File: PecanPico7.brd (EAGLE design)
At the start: 34.2 x 50 mm, 130 parts, among them IC1 Si4464-B1B-FM, IC10 TC1185-1.8VCT713, IC11 TC1185-2.5VCT713, IC12 ADR380ARTZ, IC13 AVT-55689, IC2 Si4464-B1B-FM, IC3 BME280_BME280, IC4 UBLOX_MAX-6, IC5 STM32F429IIH6, IC6 TPS61202, IC7 SPV1040, IC8 TXC_7Z, IC9 TPS62260DRVT, Q1 AP2301, U2 PAC1720-1-AIA-TR, X1 CAMERA_HEADER

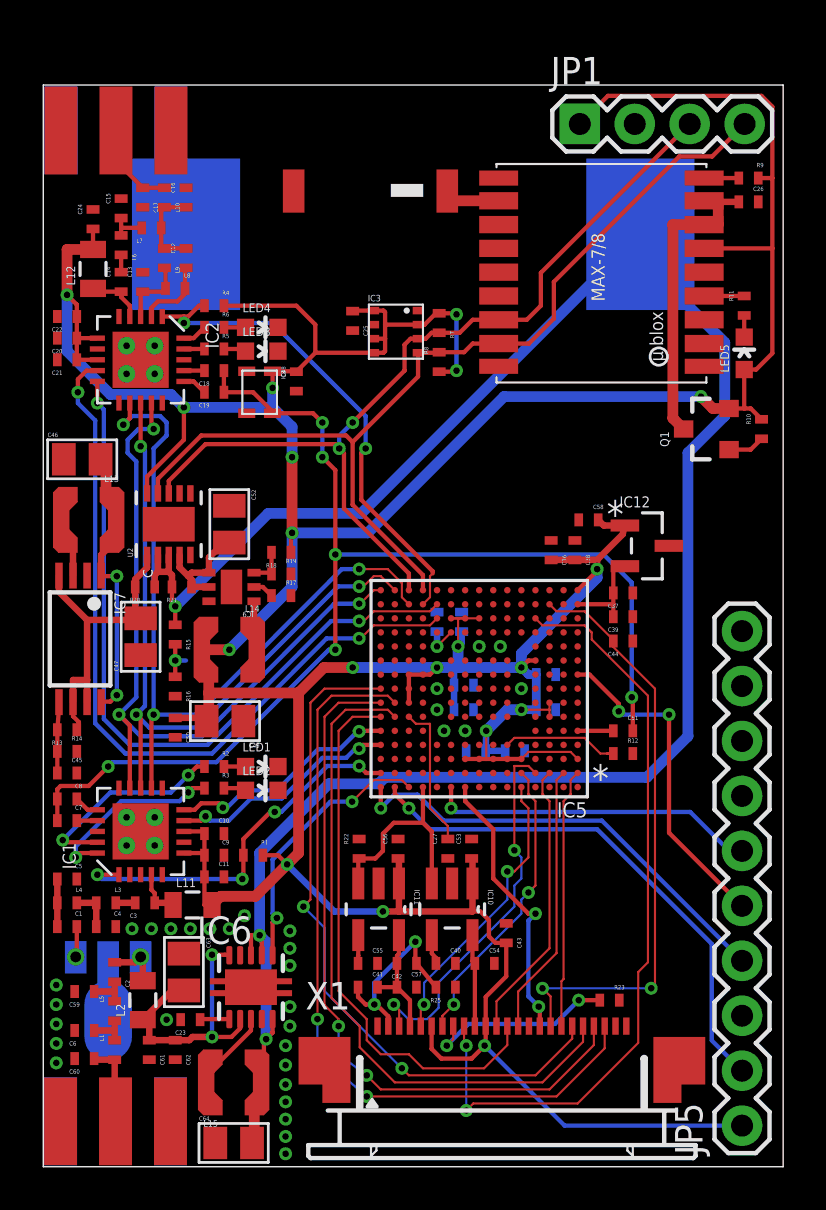
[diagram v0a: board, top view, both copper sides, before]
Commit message: Added RF6886, moved parts around
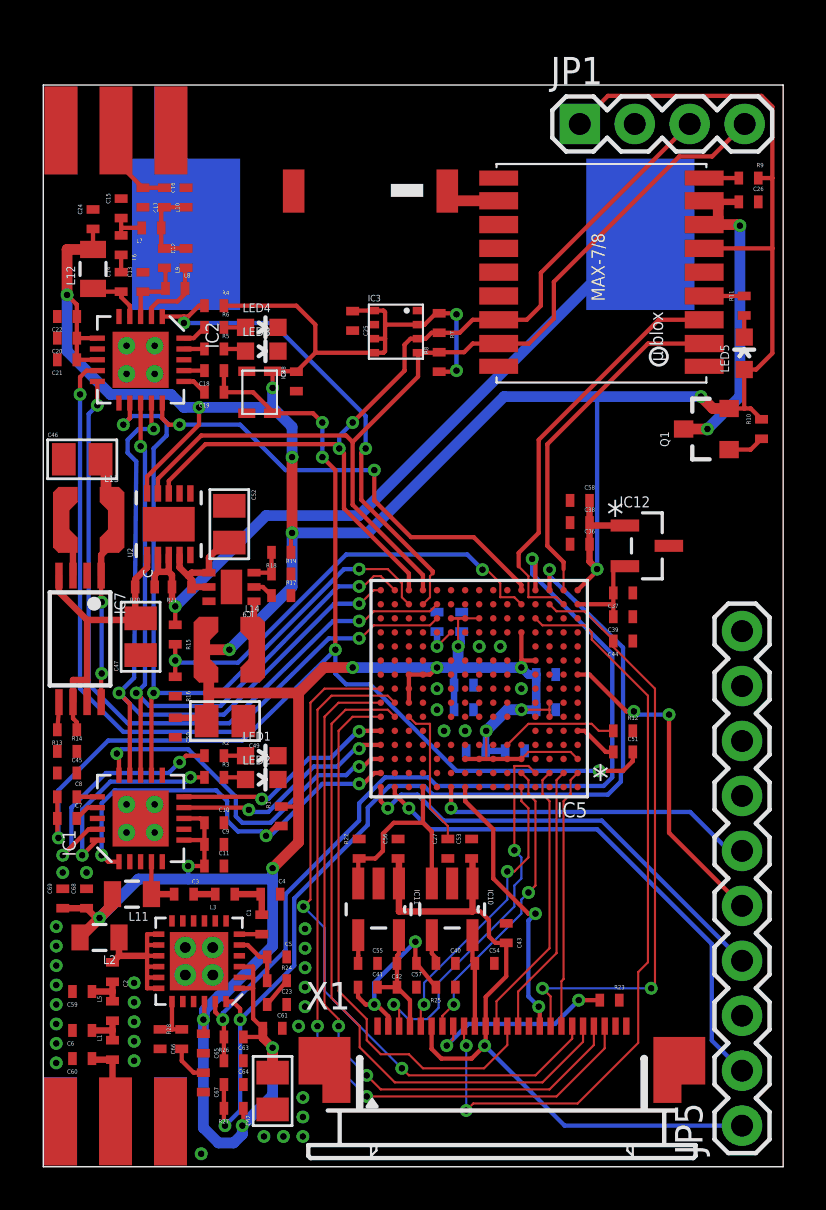
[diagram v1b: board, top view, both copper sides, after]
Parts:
- removed IC6: TPS61202, PecanPico4:S-PDSO-N10
- removed L15: LPS3015-103MRB, PecanPico6:LPS3015
- removed L4: 68nH, PecanPico6:0402
- added C65, C67: 1uF, PecanPico6:0402
- added C66, C69: 2.2uF, PecanPico6:0402
- added C68: 1nF, PecanPico6:0402
- added R24, R28: 220R, PecanPico6:0402
- added R26, R27: 390R, PecanPico6:0402
- C5: value 22pF -> 2.2uF
- C61: value 100pF -> 220pF
- C62: value 100nF -> 10uF; device PecanPico6:0402 -> PecanFemto3:0805
- C63: value 22uF -> 1uF; device PecanFemto3:0805 -> PecanPico6:0402
- C64: value 10uF -> 1uF; device PecanFemto3:0805 -> PecanPico6:0402
- IC13: value AVT-55689 -> RF6886; device stm32f42x:SOT89 -> KT5TK:QFN-24
- moved C5 10.3 mm to (10.8, 9.70)
- moved C1 9.00 mm to (10.1, 11.2), turned to 270 degrees
- moved C4 7.75 mm to (10.5, 12.6)
- moved C61 5.79 mm to (10.6, 6.40), turned to 180 degrees
- moved L3 5.51 mm to (8.40, 12.6), turned to 0 degrees
- moved C62 4.88 mm to (10.6, 3.50)
- moved C63 4.70 mm to (8.80, 4.90), turned to 180 degrees
- moved IC13 4.57 mm to (7.20, 9.50), flipped to the top
- moved C23 4.06 mm to (10.8, 7.50), turned to 180 degrees
- moved L2 3.52 mm to (2.60, 10.6), turned to 180 degrees
- moved L11 2.84 mm to (4.10, 12.6), turned to 180 degrees
- moved C64 2.70 mm to (8.80, 3.80), turned to 180 degrees
- moved R1 2.22 mm to (11.0, 16.2), turned to 270 degrees
- moved C3 1.84 mm to (6.50, 12.6), turned to 180 degrees
- moved C36 1.35 mm to (24.8, 28.8), turned to 180 degrees
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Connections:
- removed net N$45: C23.P$2, IC6.1
- removed net N$46: C61.P$2, C62.P$2, C63.2, IC6.10, IC6.2, L2.1
- removed net N$7: C2.P$2, IC13.3, L2.2
- removed net PA_EN: IC5.A13, IC6.6
- removed net UART_RXD: IC4.3_RXD1
- removed net UART_TXD: IC4.2_TXD1
- new net AM1: C23.P$2, R24.P$1
- new net AM2: C67.P$2, R28.P$2
- new net N$43: C2.P$2, IC13.13, IC13.14, IC13.15, IC13.16, IC13.17, IC13.18, L2.1
- new net PWR_REF: C64.P$2, IC13.24, IC5.R3, R27.P$1
- new net PWR_SENSE: C63.P$2, IC13.23, IC5.R4, R26.P$1
- new net UART_FROM_GPS: IC4.2_TXD1, IC5.R2
- new net UART_TO_GPS: IC4.3_RXD1, IC5.P2
- net GND: now also C62.1, C63.P$1, C64.P$1, C65.P$1, C66.P$1, C67.P$1, C68.P$1, C69.P$1, IC13.25, IC13.P$26, IC13.P$27, IC13.P$28, IC13.P$29; no longer C62.P$1, C63.1, C64.1, IC13.2, IC6.4, IC6.9, IC6.PP, IC6.PP@1, IC6.PP@2
- net N$1: now also C1.P$1; no longer L4.P$1
- net N$4: now also IC13.5, R24.P$2; no longer C1.P$2, L4.P$2
- net N$44: now also C66.P$2, IC13.19, R28.P$1; no longer IC6.3, L15.1_1, L15.1_2, L15.1_3, L15.1_4, L15.1_5, L15.1_6, L15.1_7, L15.1_8, L15.1_9
- net N$6: now also C1.P$2, IC13.6; no longer C1.P$1, IC13.1
- net RADIO1_CS: now also IC5.C15
- net RADIO2_CS: now also IC5.R5
- net VBAT: no longer C64.2, IC6.5, IC6.7, IC6.8, L15.2_1, L15.2_2, L15.2_3, L15.2_4, L15.2_5, L15.2_6, L15.2_7, L15.2_8, L15.2_9
- net VBAT_DIFF: now also IC5.P5
- net VCC: now also C61.P$2, C62.2, C65.P$2, C68.P$2, C69.P$2, IC13.1, IC13.2, IC13.22, IC13.3, IC5.M5, L2.2, R26.P$2, R27.P$2
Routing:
- net VBAT: track 99.7 -> 34.0 mm, vias 3 -> 1
- net PWR_REF: track 0.00 -> 45.4 mm, vias 0 -> 3
- net PWR_SENSE: track 0.00 -> 41.2 mm, vias 0 -> 2
- net VCC: track 240.0 -> 276.4 mm, vias 19 -> 23
- net RADIO2_CS: track 0.00 -> 21.6 mm, vias 0 -> 2
- net UART_TO_GPS: track 0.00 -> 19.6 mm
- net VBAT_DIFF: track 2.00 -> 20.9 mm, vias 1 -> 2
- net RADIO1_CS: track 0.00 -> 16.5 mm, vias 0 -> 2
- net UART_FROM_GPS: track 0.00 -> 16.2 mm
- net N$46: track 13.2 -> 0.00 mm, vias 2 -> 0
- net PA_EN: track 12.5 -> 0.00 mm, vias 2 -> 0
- net N$43: track 0.00 -> 8.44 mm
- net N$44: track 7.06 -> 2.29 mm
- net N$7: track 2.46 -> 0.00 mm, vias 1 -> 0
- net RADIO1_SDN: track 17.5 -> 20.0 mm, vias 4 -> 3
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
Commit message: Connected ADCs
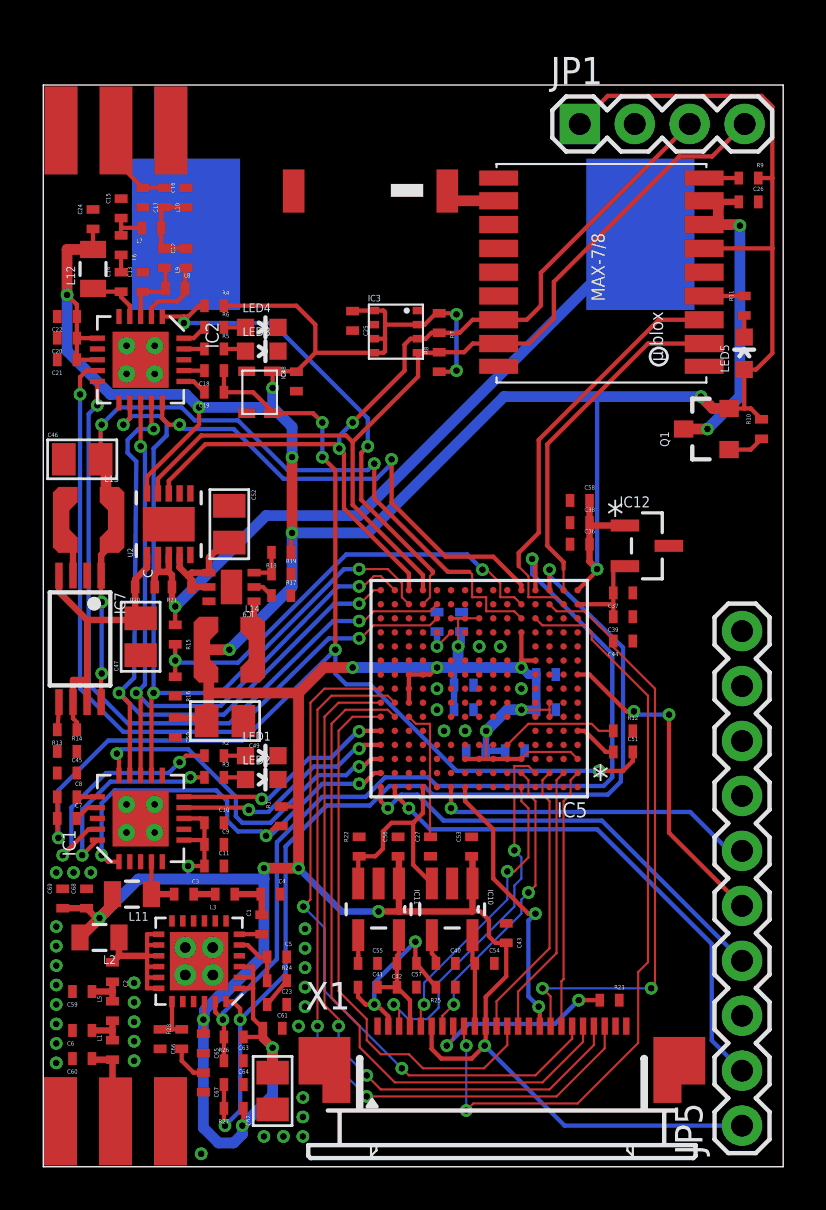
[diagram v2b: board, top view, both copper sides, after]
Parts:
- moved C27 0.81 mm to (17.9, 14.8)
- moved C53 0.10 mm to (19.8, 14.8)
- moved C56 0.10 mm to (16.4, 14.8)
- moved R22 0.10 mm to (14.6, 14.8)
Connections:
- net VSOLAR: now also IC5.N5
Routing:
- net VSOLAR: track 13.7 -> 41.4 mm, vias 2 -> 4
- net VCC: track 276.4 -> 282.6 mm, vias 23 -> 25
- net RADIO2_CS: track 21.6 -> 22.8 mm
- net PWR_SENSE: track 41.2 -> 42.4 mm
- net PWR_REF: track 45.4 -> 46.6 mm

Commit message: Connected GPS to STM32F4, moved parts around
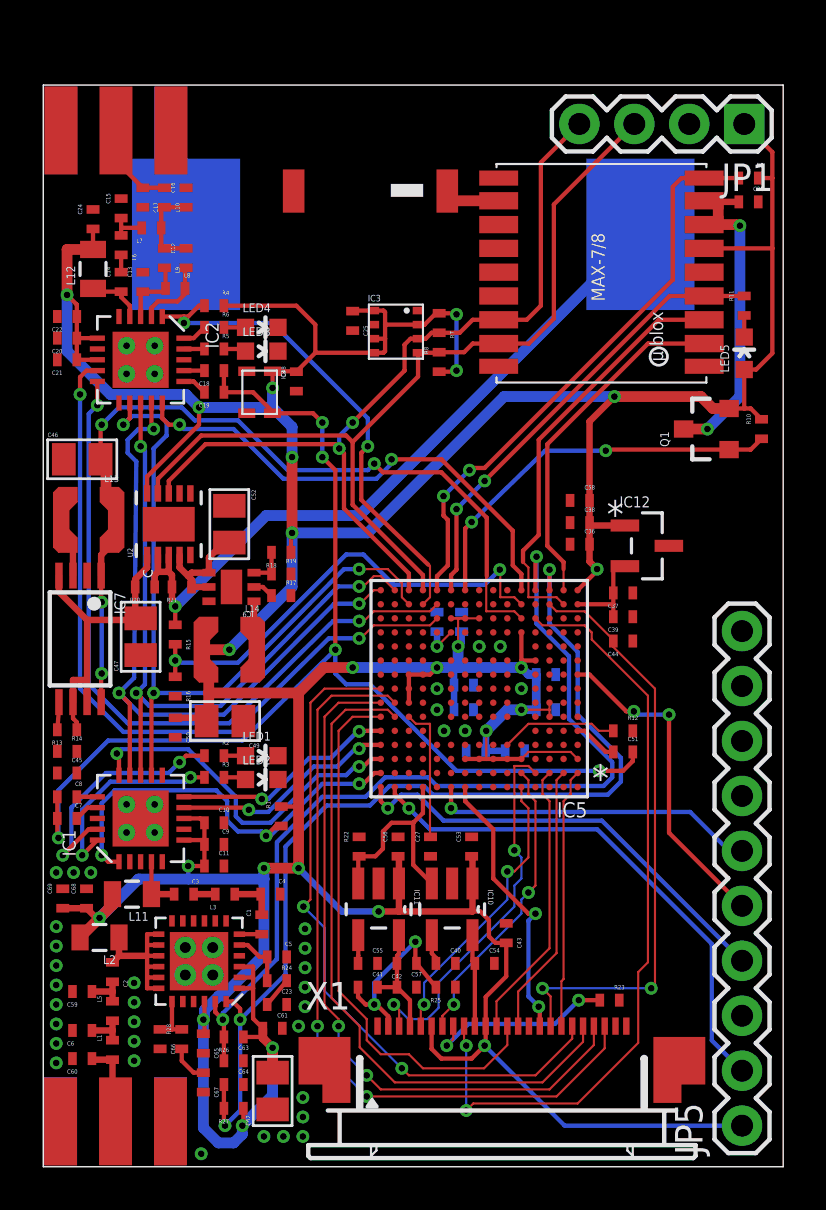
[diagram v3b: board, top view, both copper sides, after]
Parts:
- moved JP1 7.60 mm to (32.4, 48.2), turned to 180 degrees
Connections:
- new net N$7: IC5.R8
- net GPS_OFF: now also IC5.R9
- net GPS_RESET: now also IC5.R11
- net I2C_SCL: now also JP1.3; no longer JP1.4
- net I2C_SDA: now also JP1.4; no longer JP1.3
- net TIMEPULSE: now also IC5.R10
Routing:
- net GPS_RESET: track 1.60 -> 26.9 mm, vias 0 -> 2
- net TIMEPULSE: track 1.85 -> 21.2 mm, vias 0 -> 2
- net GPS_OFF: track 1.71 -> 18.2 mm, vias 0 -> 2
- net VCC: track 282.6 -> 270.0 mm
- net I2C_SCL: track 44.8 -> 41.8 mm
- net I2C_SDA: track 41.5 -> 39.4 mm
- net VBAT_DIFF: track 20.9 -> 21.9 mm
- net VSOLAR: track 41.4 -> 42.0 mm

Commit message: Many changes Added REF pullups to PA Added SD card slot Added MOSFET for SD card and camera Added Status LEDS Added capacitors for PA_PWR_REF and PA_PWR_REV Added Debug UART output Added UART to GPS moved parts around
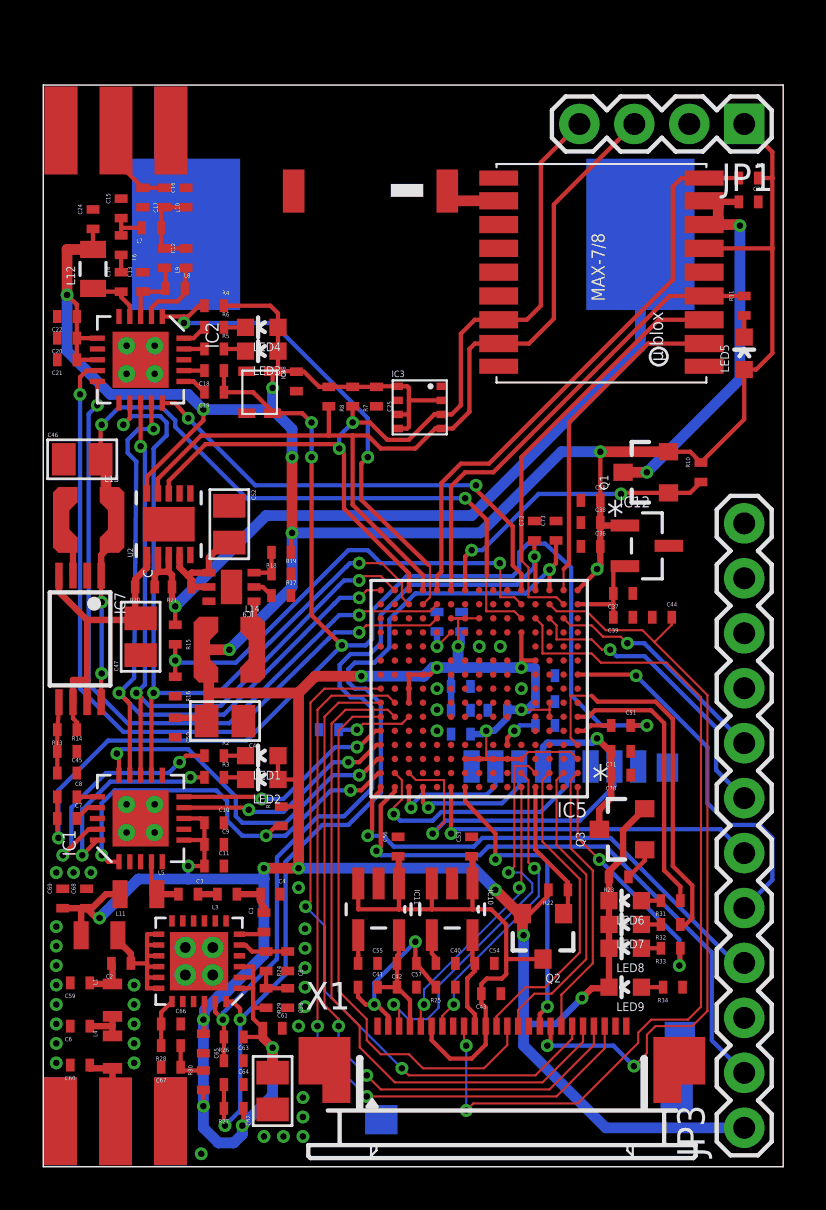
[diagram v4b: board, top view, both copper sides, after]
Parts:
- removed JP5: (no value), SparkFun-Connectors:1X10
- removed L2: (no value), PecanPico6:0805
- added C70: 100nF, PecanPico6:0402
- added C71: 2.2uF, PecanPico6:0402
- added C72, C73: 1uF, PecanPico6:0402
- added JP3: (no value), SparkFun-Connectors:1X12
- added L4: 68nH, sven:0603
- added LED6: red, PecanPico6:LED-0603
- added LED7: yellow, PecanPico6:LED-0603
- added LED8, LED9: green, PecanPico6:LED-0603
- added Q2, Q3: AP2301, PecanPico6:SOT23-3
- added R29, R30: (no value), PecanPico6:0402
- added R31, R32, R33, R34: 3.3k, PecanPico6:0402
- added U1: USD-SOCKETUSD, SparkFun-Connectors:USD-SOCKET-PP
- L1: device PecanPico6:0402 -> sven:0603
- L11: device PecanPico6:0805 -> sven:0805
- L5: value 68nH -> (none); device PecanPico6:0402 -> sven:0805
- R23: value 10k -> 47k
- moved R22 9.41 mm to (23.8, 12.8), turned to 0 degrees
- moved C27 7.16 mm to (13.2, 20.2), flipped to the bottom, turned to 0 degrees
- moved R23 5.72 mm to (26.6, 13.4), turned to 0 degrees
- moved L5 5.53 mm to (4.40, 12.6), turned to 180 degrees
- moved R8 5.35 mm to (13.2, 35.6), turned to 90 degrees
- moved R7 5.25 mm to (14.3, 35.6)
- moved C25 3.67 mm to (15.4, 35.6)
- moved IC3 3.67 mm to (17.4, 35.1)
- moved R12 3.61 mm to (23.2, 20.4), flipped to the bottom, turned to 0 degrees
- moved R10 3.44 mm to (30.4, 32.1)
- moved Q1 3.44 mm to (27.9, 32.1)
- moved C43 2.89 mm to (20.7, 8.00), turned to 0 degrees
- moved C30 2.62 mm to (19.3, 20.0), turned to 0 degrees
- moved L11 2.42 mm to (2.60, 10.7)
- moved L1 2.30 mm to (3.20, 7.70)
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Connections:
- net VCC1V8 renamed CAM_VCC1V8
- net VCC2V5 renamed CAM_VCC2V5
- removed net N$7: IC5.R8
- removed net VREG_SDN: IC10.3, IC11.3, IC5.A12, R22.P$2
- new net CAM_OFF: IC5.A4, Q2.1, R22.P$2
- new net CAM_VCC3V0: C43.P$1, C53.P$2, C56.P$2, IC10.1, IC10.3, IC11.1, IC11.3, Q2.3, X1.11, X1.6
- new net LED1: IC5.F1, R31.P$2
- new net LED2: IC5.D1, R32.P$2
- new net LED3: IC5.A1, R33.P$2
- new net N$45: JP3.10
- new net N$46: JP3.11
- new net N$47: LED6.A, R31.P$1
- new net N$48: LED7.A, R32.P$1
- new net N$49: LED8.A, R33.P$1
- new net N$50: LED9.A, R34.P$1
- new net SD_CS: IC5.A13, U1.2
- new net SD_MISO: IC5.B13, U1.7
- new net SD_MOSI: IC5.A12, U1.3
- new net SD_OFF: Q3.1, R23.P$2
- new net SD_SCK: IC5.B14, U1.5
- new net UART_RXD: IC5.N2, JP3.8
- new net UART_TXD: IC5.N3, JP3.7
- net AM1: now also R29.P$2
- net AM2: now also R30.P$1
- net GND: now also C70.P$2, C71.P$2, C72.P$1, C73.P$1, JP3.12, JP3.3, JP3.9, R34.P$2, U1.6, U1.CD1, U1.CD2, U1.GND1, U1.GND2, X1.8; no longer JP5.3, LED1.C, LED2.C, LED3.C, LED4.C, R22.P$1, R23.P$1
- net N$10: now also LED2.C, R3.P$1; no longer LED1.A, R2.P$1
- net N$11: now also LED1.C, R2.P$1; no longer LED2.A, R3.P$1
- net N$2: now also L5.P$1; no longer L11.1
- net N$21: now also LED3.C; no longer LED3.A
- net N$22: now also LED4.C; no longer LED4.A
- net N$34: now also L1.P$1; no longer L5.P$1
- net N$40: now also C70.P$1, C71.P$1, Q3.3, U1.4; no longer R23.P$2, X1.8
- net N$41: now also L4.P$2; no longer L1.P$2
- net N$43: now also L11.P$1; no longer L2.1
- net N$5: now also L1.P$2, L4.P$1; no longer L1.P$1, L5.P$2
- net NRST: now also JP3.5; no longer JP5.5
- net PWR_REF: now also C73.P$2
- net PWR_SENSE: now also C72.P$2
- net SWCLK: now also JP3.2; no longer JP5.2
- net SWDIO: now also JP3.4; no longer JP5.4
- net SWO: now also JP3.6; no longer JP5.6
- net VCC: now also JP3.1, L11.P$2, L5.P$2, LED1.A, LED2.A, LED3.A, LED4.A, LED6.C, LED7.C, LED8.C, LED9.C, Q2.2, Q3.2, R22.P$1, R23.P$1, R29.P$1, R30.P$2; no longer C43.P$1, C53.P$2, C56.P$2, IC10.1, IC11.1, JP5.1, L11.2, L2.2, X1.11, X1.6
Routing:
- net CAM_VCC3V0: track 0.00 -> 26.4 mm
- net LED2: track 0.00 -> 17.8 mm
- net SD_MISO: track 0.00 -> 14.7 mm, vias 0 -> 1
- net UART_TXD: track 0.00 -> 14.0 mm, vias 0 -> 1
- net LED1: track 0.00 -> 12.9 mm
- net SD_SCK: track 0.00 -> 11.9 mm, vias 0 -> 1
- net LED3: track 0.00 -> 11.0 mm, vias 0 -> 2
- net UART_RXD: track 0.00 -> 10.7 mm, vias 0 -> 1
- net VREG_SDN: track 9.87 -> 0.00 mm
- net CAM_PCLK: track 27.5 -> 35.4 mm
- net CLOCK: track 53.8 -> 61.5 mm
- net CAM_OFF: track 0.00 -> 6.67 mm
- net SD_MOSI: track 0.00 -> 6.57 mm, vias 0 -> 1
- net SD_CS: track 0.00 -> 6.26 mm, vias 0 -> 1
- net CAM_HREF: track 36.3 -> 41.3 mm
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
